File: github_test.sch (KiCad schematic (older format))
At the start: 1 part, among them U1 AP2112K-X.XTRG1

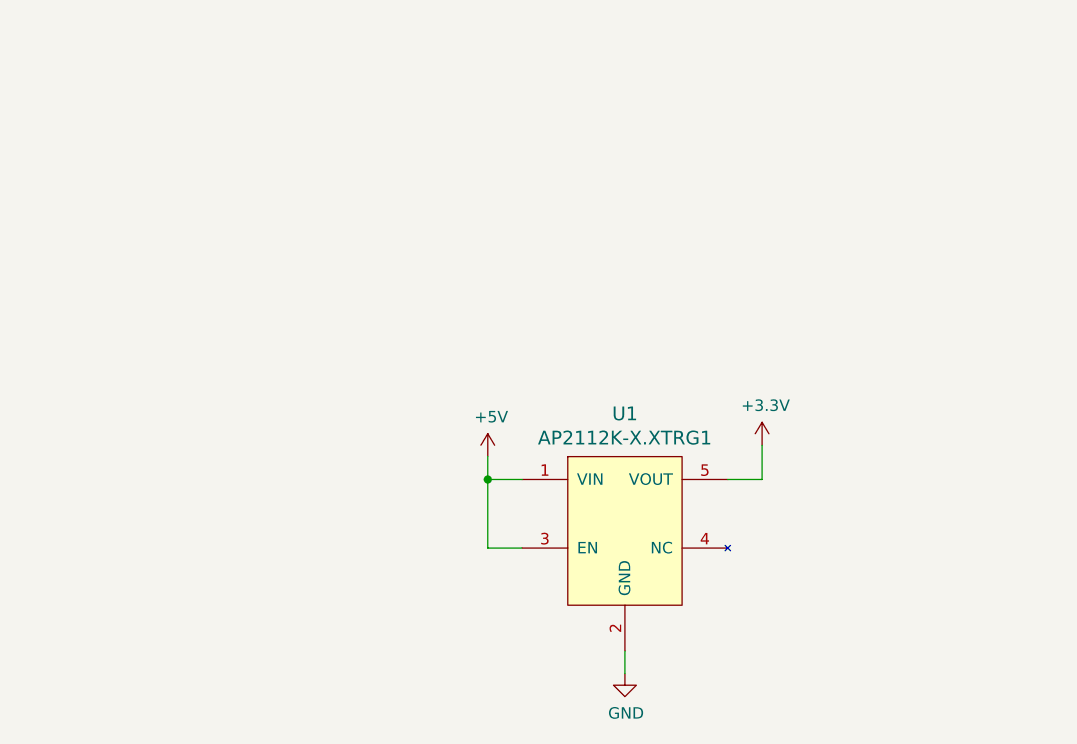
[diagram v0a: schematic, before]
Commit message: Added RJ45
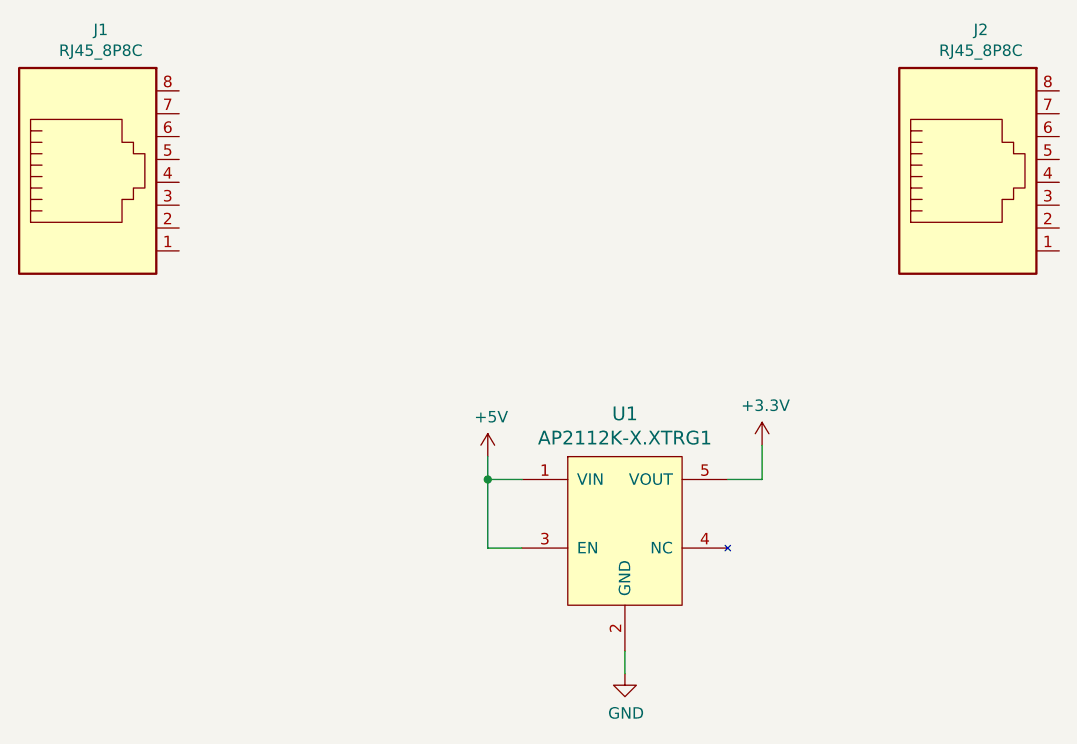
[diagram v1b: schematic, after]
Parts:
- added J1: RJ45_8P8C, KKL_connectors_RJ:RJ45_femal_connector_8P8C_Right_angle, symbol KKL_connectors:RJ45_8P8C
- added J2: RJ45_8P8C, KKL_connectors_RJ:RJ45_femal_connector_8P8C_vertical, symbol KKL_connectors:RJ45_8P8C
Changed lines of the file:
@@
 Wire Wire Line
 	5750 4150 5750 4250
+$Comp
+L KKL_connectors:RJ45_8P8C J1
+U 1 1 602358FA
+P 3400 2100
+F 0 "J1" H 3457 2767 50  0000 C CNN
+F 1 "RJ45_8P8C" H 3457 2676 50  0000 C CNN
+F 2 "KKL_connectors_RJ:RJ45_femal_connector_8P8C_Right_angle" H 3400 2100 50  0001 C CNN
+F 3 "" H 3400 2100 50  0001 C CNN
+	1    3400 2100
+	1    0    0    -1
+$EndComp
+$Comp
+L KKL_connectors:RJ45_8P8C J2
+U 1 1 602361CB
+P 7250 2100
+F 0 "J2" H 7307 2767 50  0000 C CNN
+F 1 "RJ45_8P8C" H 7307 2676 50  0000 C CNN
+F 2 "KKL_connectors_RJ:RJ45_femal_connector_8P8C_vertical" H 7250 2100 50  0001 C CNN
+F 3 "" H 7250 2100 50  0001 C CNN
+	1    7250 2100
+	1    0    0    -1
+$EndComp
 $EndSCHEMATC
